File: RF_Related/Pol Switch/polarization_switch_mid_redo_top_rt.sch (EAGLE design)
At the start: 53 parts, among them IC1 VLPR-24-858-2, IC10 ADP-2-1+_MINICIRCUITS, IC11 ADP-2-1+_MINICIRCUITS, IC12 QCV-151+, IC13 MAX8878EUK28+T, IC14 SN74LVC2G17DBVT, IC15 SN74LVC2G17DBVT, IC2 VLPR-24-858-2, IC3 HSWA2-30DR+, IC4 VLPR-24-858-2, IC5 HSWA2-30DR+, IC6 HSWA2-30DR+, IC7 HSWA2-30DR+, IC8 PHA-13LN+, IC9 PHA-13LN+, J1 M20-9730645, J2 171856-0002, X1 SMA-142-0701-801/806, X2 SMA-142-0701-801/806, X3 SMA-142-0701-801/806

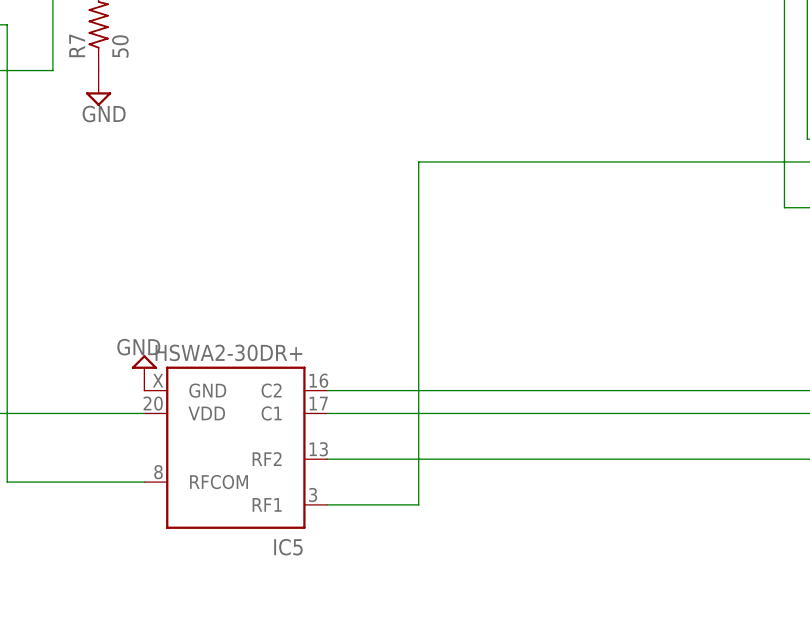
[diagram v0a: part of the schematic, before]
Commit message: made a new version of the pol switch. already sent to OSH park for fab. note that there is a template for routing as well as a completed circuit
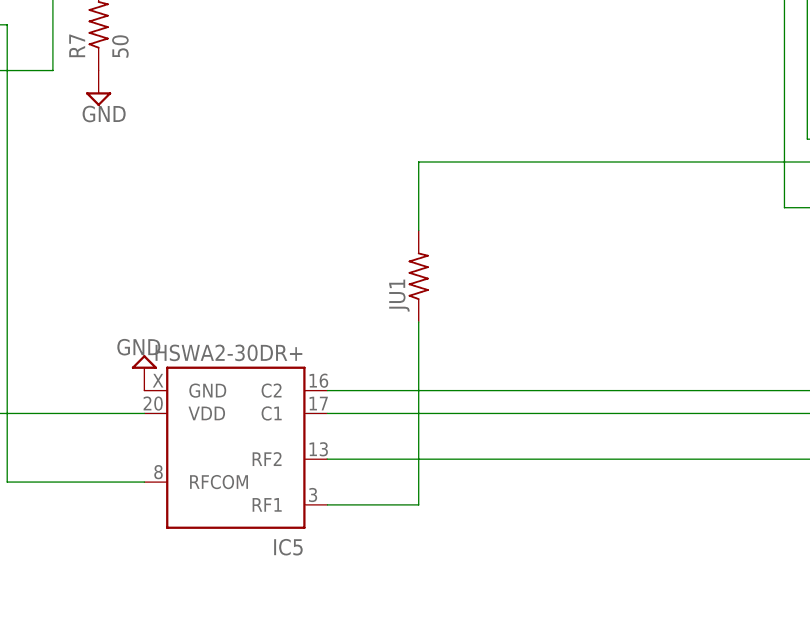
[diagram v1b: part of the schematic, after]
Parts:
- added JU1: (no value), rcl_jumper_pads:R-US_R1206
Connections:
- new net N$10: IC11.PORT_2, JU1.2
- net N$12: now also JU1.1; no longer IC11.PORT_2
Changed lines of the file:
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@@
 <part name="C2" library="rcl" library_urn="urn:adsk.eagle:library:334" deviceset="C-US" device="C0603" package3d_urn="urn:adsk.eagle:package:23616/2" value="1e-9"/>
 <part name="SUPPLY3" library="supply2" library_urn="urn:adsk.eagle:library:372" deviceset="GND" device=""/>
+<part name="JU1" library="rcl_jumper_pads" deviceset="R-US_" device="R1206" package3d_urn="urn:adsk.eagle:package:23540/2"/>
 </parts>
 <sheets>
@@
 <instance part="SUPPLY3" gate="GND" x="358.14" y="101.6" smashed="yes">
 <attribute name="VALUE" x="356.235" y="98.425" size="1.778" layer="96"/>
+</instance>
+<instance part="JU1" gate="G$1" x="101.6" y="93.98" smashed="yes" rot="R90">
+<attribute name="NAME" x="100.1014" y="90.17" size="1.778" layer="95" rot="R90"/>
+<attribute name="VALUE" x="104.902" y="90.17" size="1.778" layer="96" rot="R90"/>
 </instance>
 </instances>
@@
 </segment>
 </net>
+<net name="N$10" class="0">
+<segment>
+<pinref part="IC11" gate="G$1" pin="PORT_2"/>
+<wire x1="101.6" y1="106.68" x2="200.66" y2="106.68" width="0.1524" layer="91"/>
+<wire x1="200.66" y1="106.68" x2="200.66" y2="137.16" width="0.1524" layer="91"/>
+<wire x1="101.6" y1="99.06" x2="101.6" y2="106.68" width="0.1524" layer="91"/>
+<pinref part="JU1" gate="G$1" pin="2"/>
+</segment>
+</net>
 <net name="N$4" class="0">
 <segment>
@@
 <pinref part="IC5" gate="G$1" pin="RF1"/>
 <wire x1="101.6" y1="68.58" x2="91.44" y2="68.58" width="0.1524" layer="91"/>
-<wire x1="101.6" y1="68.58" x2="101.6" y2="106.68" width="0.1524" layer="91"/>
-<pinref part="IC11" gate="G$1" pin="PORT_2"/>
-<wire x1="101.6" y1="106.68" x2="200.66" y2="106.68" width="0.1524" layer="91"/>
-<wire x1="200.66" y1="106.68" x2="200.66" y2="137.16" width="0.1524" layer="91"/>
+<wire x1="101.6" y1="68.58" x2="101.6" y2="88.9" width="0.1524" layer="91"/>
+<pinref part="JU1" gate="G$1" pin="1"/>
 </segment>
 </net>
@@
 will not be understood (or retained) with this version.
 </note>
+<note version="8.4" severity="warning">
+Since Version 8.4, EAGLE supports properties for SPICE simulation.
+Probes in schematics and SPICE mapping objects found in parts and library devices
+will not be understood with this version. Update EAGLE to the latest version
+for full support of SPICE simulation.
+</note>
 </compatibility>
